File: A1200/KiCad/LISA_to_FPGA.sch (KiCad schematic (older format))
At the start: 39 parts, among them J1 Conn_01x01, J2 Conn_01x40, U1 LM1117-3.3, U2 74LVC162244ADGG, U3 74LVC162244ADGG, U4 LISA, U5 RP2354B

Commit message: Add decoupling cap for pin 59,60 on QFN-80 footprint, and change Csync pin hole to 0.8 mm
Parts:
- added C20: 0.1uF, Capacitor_SMD:C_0603_1608Metric_Pad1.08x0.95mm_HandSolder, symbol Device:C_Small
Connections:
- net 3V3: now also C20.2
- net GND: now also C20.1
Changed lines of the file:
@@
 Connection ~ 5650 7250
 Wire Wire Line
-	5650 7250 6600 7250
+	5650 7250 5950 7250
+$Comp
+L Device:C_Small C20
+U 1 1 6B0FEB9C
+P 5950 7150
+F 0 "C20" H 6042 7196 50  0000 L CNN
+F 1 "0.1uF" H 6000 7300 50  0000 L CNN
+F 2 "Capacitor_SMD:C_0603_1608Metric_Pad1.08x0.95mm_HandSolder" H 5950 7150 50  0001 C CNN
+F 3 "~" H 5950 7150 50  0001 C CNN
+	1    5950 7150
+	1    0    0    -1
+$EndComp
+Connection ~ 5950 7250
+Wire Wire Line
+	5950 7250 6600 7250
+Wire Wire Line
+	5950 7050 5950 6900
+Wire Wire Line
+	5950 6900 5650 6900
+Connection ~ 5650 6900
 $EndSCHEMATC

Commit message: Add decoupling cap for pin 51 on QFN-80 footprint
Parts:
- added C21: 0.1uF, Capacitor_SMD:C_0603_1608Metric_Pad1.08x0.95mm_HandSolder, symbol Device:C_Small
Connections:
- net 1V1: now also C21.2
- net GND: now also C21.1
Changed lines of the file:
@@
 1V1
 Wire Wire Line
-	3100 7700 2050 7700
+	3100 7700 2350 7700
 Wire Wire Line
 	1300 7550 1850 7550
@@
 Connection ~ 2050 7400
 Wire Wire Line
-	2050 7400 3100 7400
+	2050 7400 2350 7400
 $Comp
 L Device:C_Small C19
@@
 	5950 6900 5650 6900
 Connection ~ 5650 6900
+$Comp
+L Device:C_Small C21
+U 1 1 6B11C11D
+P 2350 7600
+F 0 "C21" H 2442 7646 50  0000 L CNN
+F 1 "0.1uF" H 2400 7750 50  0000 L CNN
+F 2 "Capacitor_SMD:C_0603_1608Metric_Pad1.08x0.95mm_HandSolder" H 2350 7600 50  0001 C CNN
+F 3 "~" H 2350 7600 50  0001 C CNN
+	1    2350 7600
+	1    0    0    -1
+$EndComp
+Connection ~ 2350 7700
+Wire Wire Line
+	2350 7700 2050 7700
+Wire Wire Line
+	2350 7400 2350 7500
+Connection ~ 2350 7400
+Wire Wire Line
+	2350 7400 3100 7400
 $EndSCHEMATC

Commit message: Add external pull-up resistor on strapping pin GPIO33
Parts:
- added C22: 0.1uF, Capacitor_SMD:C_0603_1608Metric_Pad1.08x0.95mm_HandSolder, symbol Device:C_Small
- added R7: 4k7, Resistor_SMD:R_0603_1608Metric_Pad0.98x0.95mm_HandSolder, symbol Device:R_Small
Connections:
- net 3V3: now also C22.2, R7.1
- net GND: now also U5.40 (GPIO32), C22.1
- net STRAP1: now reaches U5.42 (GPIO33)
- net STRAP1: now also R7.2
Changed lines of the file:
@@
 Connection ~ 5950 7250
 Wire Wire Line
-	5950 7250 6600 7250
+	5950 7250 6250 7250
 Wire Wire Line
 	5950 7050 5950 6900
@@
 Wire Wire Line
 	2350 7400 3100 7400
+$Comp
+L Device:C_Small C22
+U 1 1 6B154826
+P 6250 7150
+F 0 "C22" H 6342 7196 50  0000 L CNN
+F 1 "0.1uF" H 6300 7300 50  0000 L CNN
+F 2 "Capacitor_SMD:C_0603_1608Metric_Pad1.08x0.95mm_HandSolder" H 6250 7150 50  0001 C CNN
+F 3 "~" H 6250 7150 50  0001 C CNN
+	1    6250 7150
+	1    0    0    -1
+$EndComp
+Connection ~ 6250 7250
+Wire Wire Line
+	6250 7250 6600 7250
+Wire Wire Line
+	6250 7050 6250 6900
+Wire Wire Line
+	6250 6900 5950 6900
+Connection ~ 5950 6900
+Wire Wire Line
+	4500 5800 3900 5800
+Text Label 4000 5800 0    50   ~ 0
+STRAP0
+Text Label 5400 6350 0    50   ~ 0
+STRAP1
+$Comp
+L Device:R_Small R7
+U 1 1 6B1787D1
+P 5400 6500
+F 0 "R7" H 5459 6500 50  0000 L CNN
+F 1 "4k7" H 5200 6500 50  0000 L CNN
+F 2 "Resistor_SMD:R_0603_1608Metric_Pad0.98x0.95mm_HandSolder" H 5400 6500 50  0001 C CNN
+F 3 "~" H 5400 6500 50  0001 C CNN
+	1    5400 6500
+	-1   0    0    1
+$EndComp
+Wire Wire Line
+	5400 6600 5400 6650
+Wire Wire Line
+	5400 6650 5200 6650
+Text GLabel 5200 6650 0    50   Input ~ 0
+3V3
+Wire Wire Line
+	5400 6200 5400 6400
+Text GLabel 3900 5800 0    50   Input ~ 0
+GND
 $EndSCHEMATC

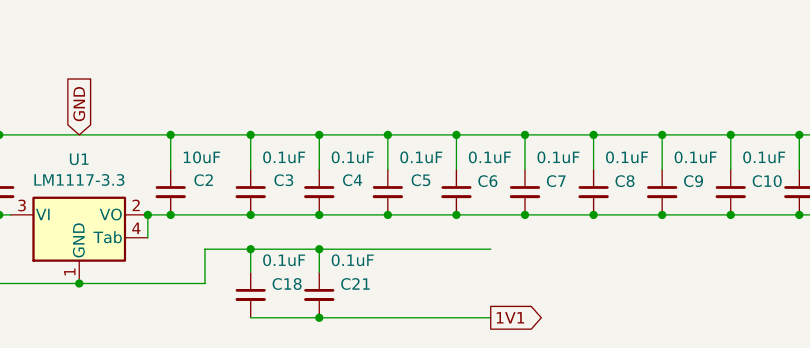
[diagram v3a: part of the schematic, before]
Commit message: Add decoupling cap for pin 10 on QFN-80 footprint
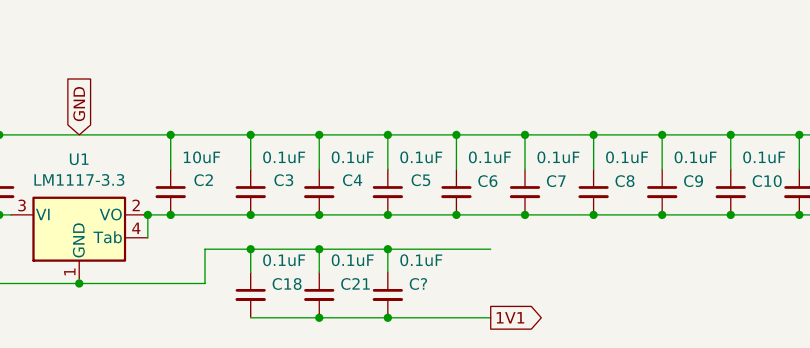
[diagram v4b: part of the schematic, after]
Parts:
- added C?: 0.1uF, Capacitor_SMD:C_0603_1608Metric_Pad1.08x0.95mm_HandSolder, symbol Device:C_Small
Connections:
- net 1V1: now also C?.2
- net GND: now also C?.1
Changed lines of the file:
@@
 1V1
 Wire Wire Line
-	3100 7700 2350 7700
+	3100 7700 2650 7700
 Wire Wire Line
 	1300 7550 1850 7550
@@
 Connection ~ 2350 7400
 Wire Wire Line
-	2350 7400 3100 7400
+	2350 7400 2650 7400
 $Comp
 L Device:C_Small C22
@@
 Text GLabel 3900 5800 0    50   Input ~ 0
 GND
+$Comp
+L Device:C_Small C?
+U 1 1 6B1BDCA0
+P 2650 7600
+F 0 "C?" H 2742 7646 50  0000 L CNN
+F 1 "0.1uF" H 2700 7750 50  0000 L CNN
+F 2 "Capacitor_SMD:C_0603_1608Metric_Pad1.08x0.95mm_HandSolder" H 2650 7600 50  0001 C CNN
+F 3 "~" H 2650 7600 50  0001 C CNN
+	1    2650 7600
+	1    0    0    -1
+$EndComp
+Connection ~ 2650 7700
+Wire Wire Line
+	2650 7700 2350 7700
+Wire Wire Line
+	2650 7400 2650 7500
+Connection ~ 2650 7400
+Wire Wire Line
+	2650 7400 3100 7400
 $EndSCHEMATC

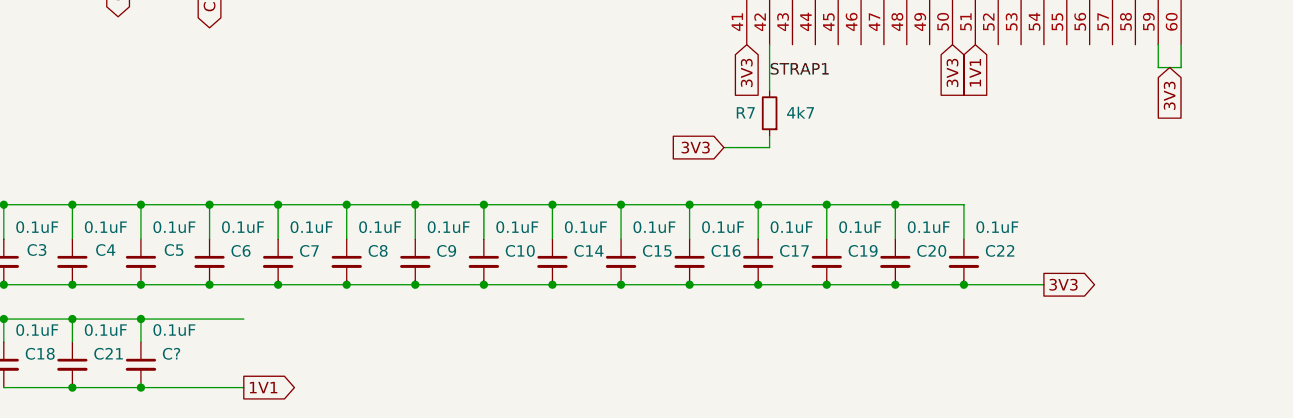
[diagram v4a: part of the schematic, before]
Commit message: Add 100nF decoupling cap for pin 64 (VREG_VIN) on QFN-80 footprint
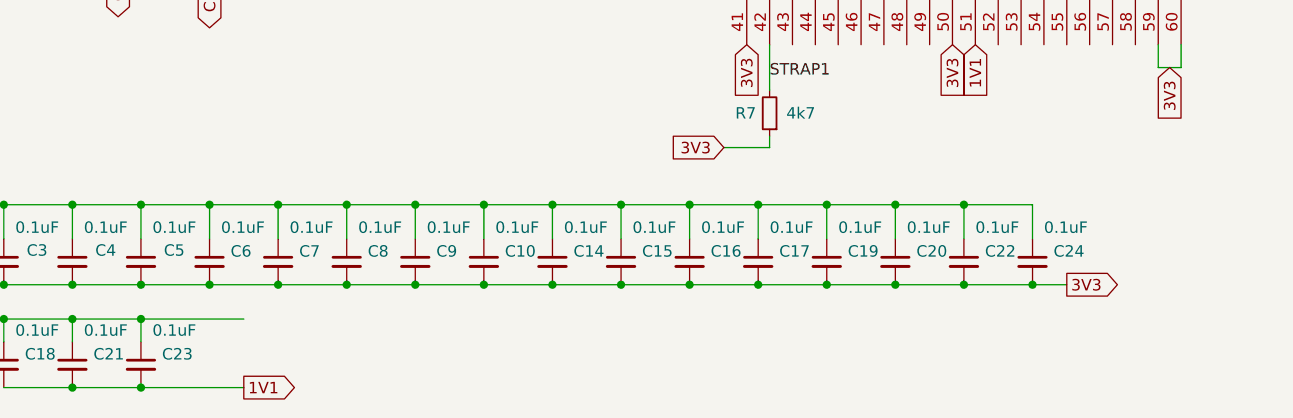
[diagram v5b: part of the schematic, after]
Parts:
- added C24: 0.1uF, Capacitor_SMD:C_0603_1608Metric_Pad1.08x0.95mm_HandSolder, symbol Device:C_Small
- gave numbers to parts that had none: 1
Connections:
- net 3V3: now also C24.2
- net GND: now also C24.1
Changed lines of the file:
@@
 	1    0    0    -1
 $EndComp
-Text GLabel 6600 7250 2    50   Output ~ 0
+Text GLabel 6700 7250 2    50   Output ~ 0
 3V3
 Connection ~ 1600 7250
@@
 Connection ~ 6250 7250
 Wire Wire Line
-	6250 7250 6600 7250
-Wire Wire Line
 	6250 7050 6250 6900
 Wire Wire Line
@@
 GND
 $Comp
-L Device:C_Small C?
+L Device:C_Small C23
 U 1 1 6B1BDCA0
 P 2650 7600
-F 0 "C?" H 2742 7646 50  0000 L CNN
+F 0 "C23" H 2742 7646 50  0000 L CNN
 F 1 "0.1uF" H 2700 7750 50  0000 L CNN
 F 2 "Capacitor_SMD:C_0603_1608Metric_Pad1.08x0.95mm_HandSolder" H 2650 7600 50  0001 C CNN
@@
 Wire Wire Line
 	2650 7400 3100 7400
+Wire Wire Line
+	6250 7250 6550 7250
+$Comp
+L Device:C_Small C24
+U 1 1 6B1D725E
+P 6550 7150
+F 0 "C24" H 6642 7196 50  0000 L CNN
+F 1 "0.1uF" H 6600 7300 50  0000 L CNN
+F 2 "Capacitor_SMD:C_0603_1608Metric_Pad1.08x0.95mm_HandSolder" H 6550 7150 50  0001 C CNN
+F 3 "~" H 6550 7150 50  0001 C CNN
+	1    6550 7150
+	1    0    0    -1
+$EndComp
+Connection ~ 6550 7250
+Wire Wire Line
+	6550 7250 6700 7250
+Wire Wire Line
+	6550 7050 6550 6900
+Wire Wire Line
+	6550 6900 6250 6900
+Connection ~ 6250 6900
 $EndSCHEMATC

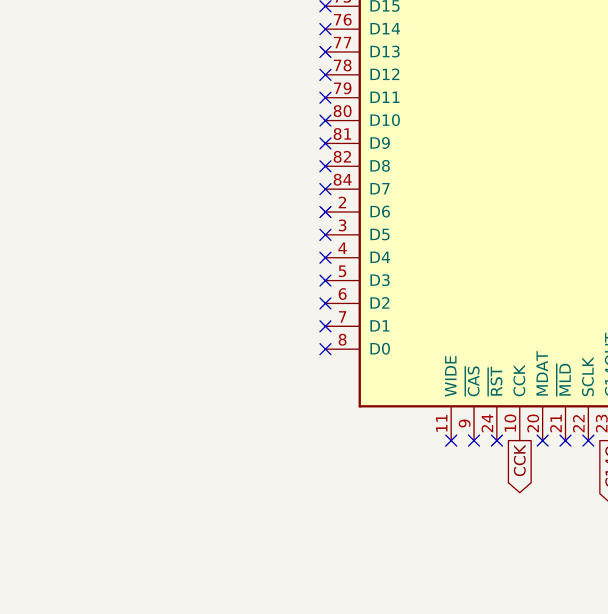
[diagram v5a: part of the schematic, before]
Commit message: Add Micro-USB connector to the design
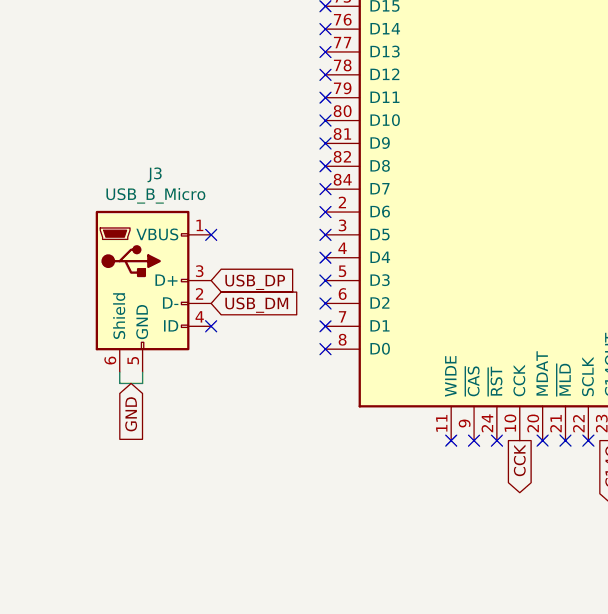
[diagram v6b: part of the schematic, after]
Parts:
- added J3: USB_B_Micro, LISA_to_FPGA:101181940001LF, symbol Connector:USB_B_Micro
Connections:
- net GND: now also J3.5 (GND), J3.6 (Shield)
- net USB_DM: now also J3.2 (D-)
- net USB_DP: now also J3.3 (D+)
- no-connect marks 43 -> 45
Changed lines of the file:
@@
 	6550 6900 6250 6900
 Connection ~ 6250 6900
+$Comp
+L Connector:USB_B_Micro J3
+U 1 1 6B218FB7
+P 900 5150
+F 0 "J3" H 957 5617 50  0000 C CNN
+F 1 "USB_B_Micro" H 957 5526 50  0000 C CNN
+F 2 "LISA_to_FPGA:101181940001LF" H 1050 5100 50  0001 C CNN
+F 3 "~" H 1050 5100 50  0001 C CNN
+	1    900  5150
+	1    0    0    -1
+$EndComp
+NoConn ~ 1200 4950
+NoConn ~ 1200 5350
+Text GLabel 850  5600 3    50   Input ~ 0
+GND
+Wire Wire Line
+	800  5550 800  5600
+Wire Wire Line
+	900  5550 900  5600
+Wire Wire Line
+	800  5600 900  5600
+Text GLabel 1200 5150 2    50   Input ~ 0
+USB_DP
+Text GLabel 1200 5250 2    50   Input ~ 0
+USB_DM
 $EndSCHEMATC

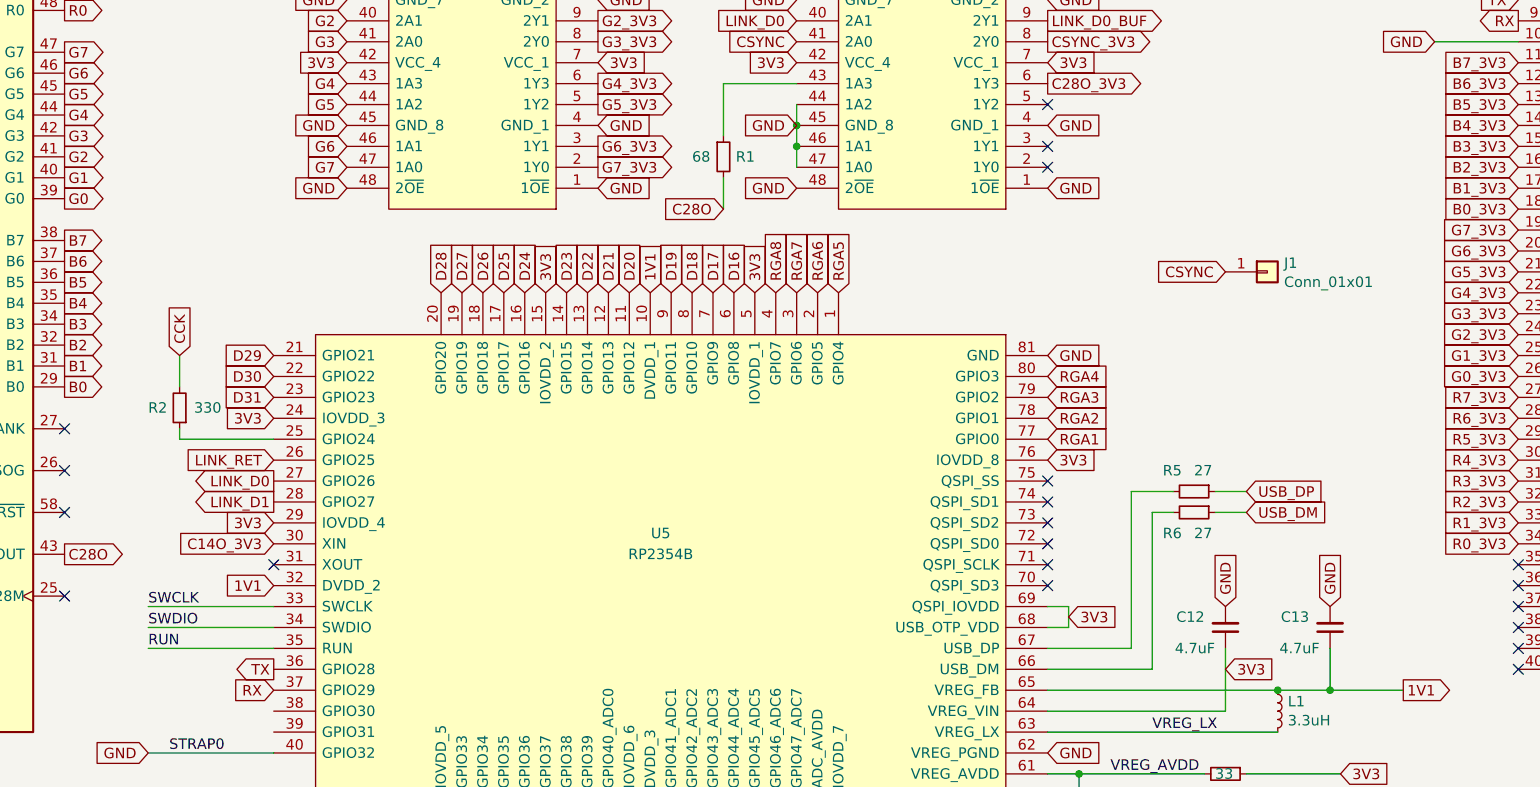
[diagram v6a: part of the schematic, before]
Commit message: Add a three-pin DEBUG-header with SWDIO,GND,SWCLK
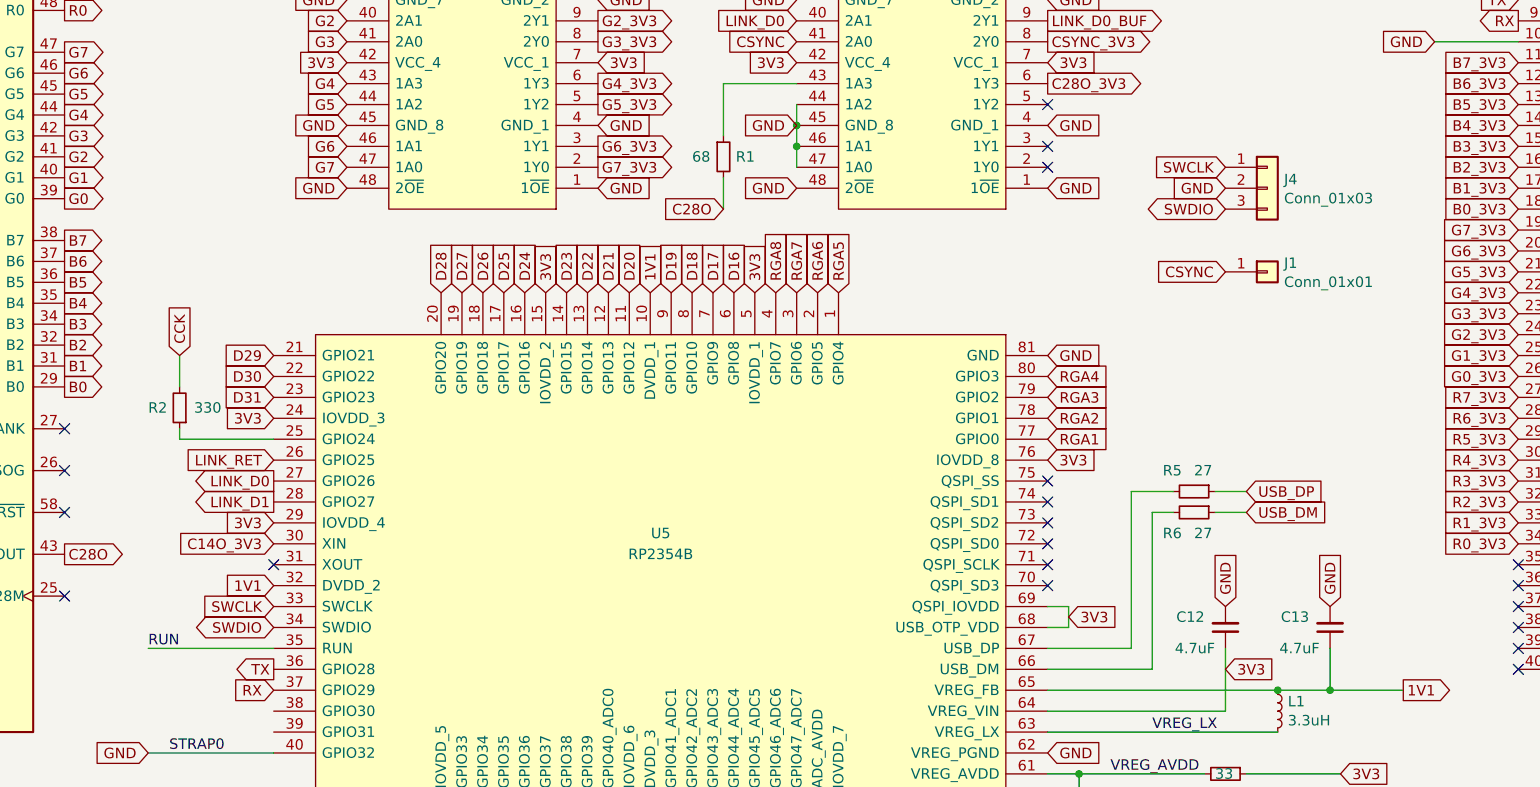
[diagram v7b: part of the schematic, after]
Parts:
- added J4: Conn_01x03, Connector_PinHeader_2.54mm:PinHeader_1x03_P2.54mm_Vertical, symbol Connector_Generic:Conn_01x03
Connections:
- net GND: now also J4.2 (Pin_2)
- net SWCLK: now also J4.1 (Pin_1)
- net SWDIO: now also J4.3 (Pin_3)
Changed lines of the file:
@@
 NoConn ~ 4500 4900
-Wire Wire Line
-	3900 5100 4500 5100
-Wire Wire Line
-	4500 5200 3900 5200
-Text Label 3900 5100 0    50   ~ 0
-SWCLK
-Text Label 3900 5200 0    50   ~ 0
-SWDIO
 Wire Wire Line
 	4500 5300 3900 5300
@@
 Text GLabel 1200 5250 2    50   Input ~ 0
 USB_DM
+$Comp
+L Connector_Generic:Conn_01x03 J4
+U 1 1 6B2518C2
+P 9250 3100
+F 0 "J4" H 9330 3142 50  0000 L CNN
+F 1 "Conn_01x03" H 9330 3051 50  0000 L CNN
+F 2 "Connector_PinHeader_2.54mm:PinHeader_1x03_P2.54mm_Vertical" H 9250 3100 50  0001 C CNN
+F 3 "~" H 9250 3100 50  0001 C CNN
+	1    9250 3100
+	1    0    0    -1
+$EndComp
+Text GLabel 9050 3100 0    50   Input ~ 0
+GND
+Text GLabel 4500 5100 0    50   Input ~ 0
+SWCLK
+Text GLabel 9050 3000 0    50   Input ~ 0
+SWCLK
+Text GLabel 9050 3200 0    50   BiDi ~ 0
+SWDIO
+Text GLabel 4500 5200 0    50   BiDi ~ 0
+SWDIO
 $EndSCHEMATC

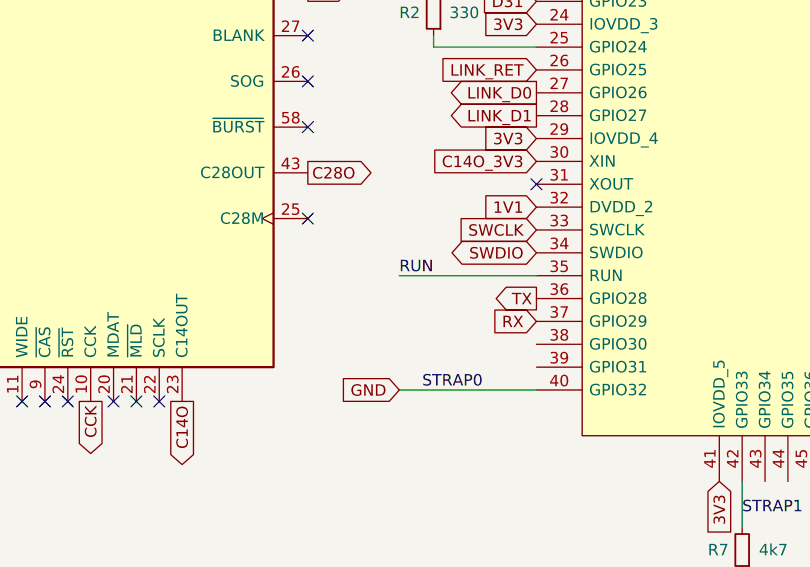
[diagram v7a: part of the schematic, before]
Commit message: Add a RESET push button
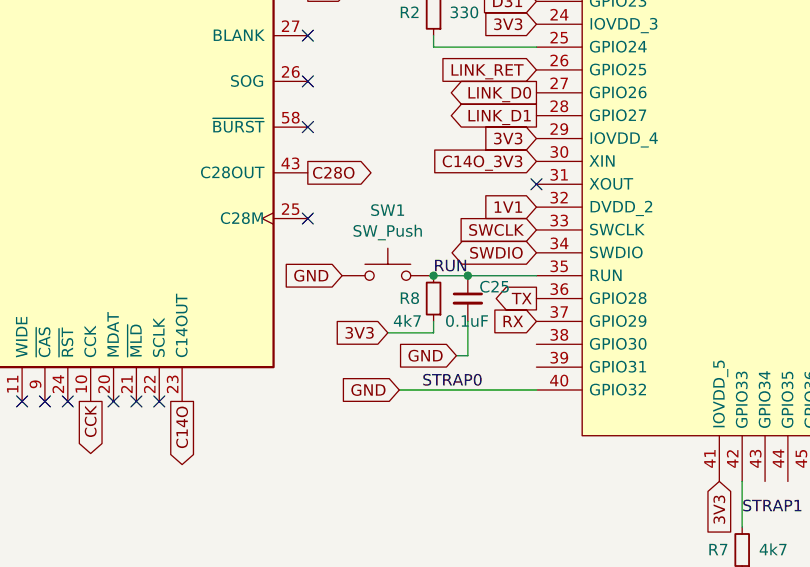
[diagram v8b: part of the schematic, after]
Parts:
- added C25: 0.1uF, Capacitor_SMD:C_0603_1608Metric_Pad1.08x0.95mm_HandSolder, symbol Device:C_Small
- added R8: 4k7, Resistor_SMD:R_0603_1608Metric_Pad0.98x0.95mm_HandSolder, symbol Device:R_Small
- added SW1: SW_Push, LISA_to_FPGA:Sunrom_Tactile_Switch_3x4x2mm_SMD_2-Pin, symbol Switch:SW_Push
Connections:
- net 3V3: now also R8.1
- net GND: now also C25.2, SW1.1
- net RUN: now also C25.1, R8.2, SW1.2
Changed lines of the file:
@@
 	8300 5100 8300 5200
 NoConn ~ 4500 4900
-Wire Wire Line
-	4500 5300 3900 5300
-Text Label 3900 5300 0    50   ~ 0
+Text Label 4050 5300 0    50   ~ 0
 RUN
 Wire Wire Line
@@
 Text GLabel 4500 5200 0    50   BiDi ~ 0
 SWDIO
+$Comp
+L Switch:SW_Push SW1
+U 1 1 6B2EABBF
+P 3850 5300
+F 0 "SW1" H 3850 5585 50  0000 C CNN
+F 1 "SW_Push" H 3850 5494 50  0000 C CNN
+F 2 "LISA_to_FPGA:Sunrom_Tactile_Switch_3x4x2mm_SMD_2-Pin" H 3850 5500 50  0001 C CNN
+F 3 "~" H 3850 5500 50  0001 C CNN
+	1    3850 5300
+	1    0    0    -1
+$EndComp
+Wire Wire Line
+	4050 5300 4200 5300
+Text GLabel 3650 5300 0    50   Input ~ 0
+GND
+$Comp
+L Device:R_Small R8
+U 1 1 6ACE19E8
+P 4050 5400
+F 0 "R8" H 4109 5400 50  0000 L CNN
+F 1 "4k7" H 4100 5500 50  0000 L CNN
+F 2 "Resistor_SMD:R_0603_1608Metric_Pad0.98x0.95mm_HandSolder" H 4050 5400 50  0001 C CNN
+F 3 "~" H 4050 5400 50  0001 C CNN
+	1    4050 5400
+	-1   0    0    1
+$EndComp
+Connection ~ 4050 5300
+Wire Wire Line
+	4050 5550 3850 5550
+Text GLabel 3850 5550 0    50   Input ~ 0
+3V3
+Wire Wire Line
+	4050 5500 4050 5550
+$Comp
+L Device:C_Small C25
+U 1 1 6AD0AEDA
+P 4200 5400
+F 0 "C25" H 4250 5450 50  0000 L CNN
+F 1 "0.1uF" H 4100 5300 50  0000 L CNN
+F 2 "Capacitor_SMD:C_0603_1608Metric_Pad1.08x0.95mm_HandSolder" H 4200 5400 50  0001 C CNN
+F 3 "~" H 4200 5400 50  0001 C CNN
+	1    4200 5400
+	1    0    0    -1
+$EndComp
+Connection ~ 4200 5300
+Wire Wire Line
+	4200 5300 4500 5300
+Text GLabel 4150 5650 0    50   Input ~ 0
+GND
+Wire Wire Line
+	4200 5650 4150 5650
+Wire Wire Line
+	4200 5500 4200 5650
 $EndSCHEMATC
